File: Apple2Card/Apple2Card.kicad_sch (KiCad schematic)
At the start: 69 parts, among them J1 ICSP, J2 Conn_01x25, J3 Conn_01x25, J4 Conn_01x16, J5 SERCON, J6 WIZNET 5500, SW1 SW_Push, U1 ATmega328P-P, U2 74HCT32, U3 74HCT00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

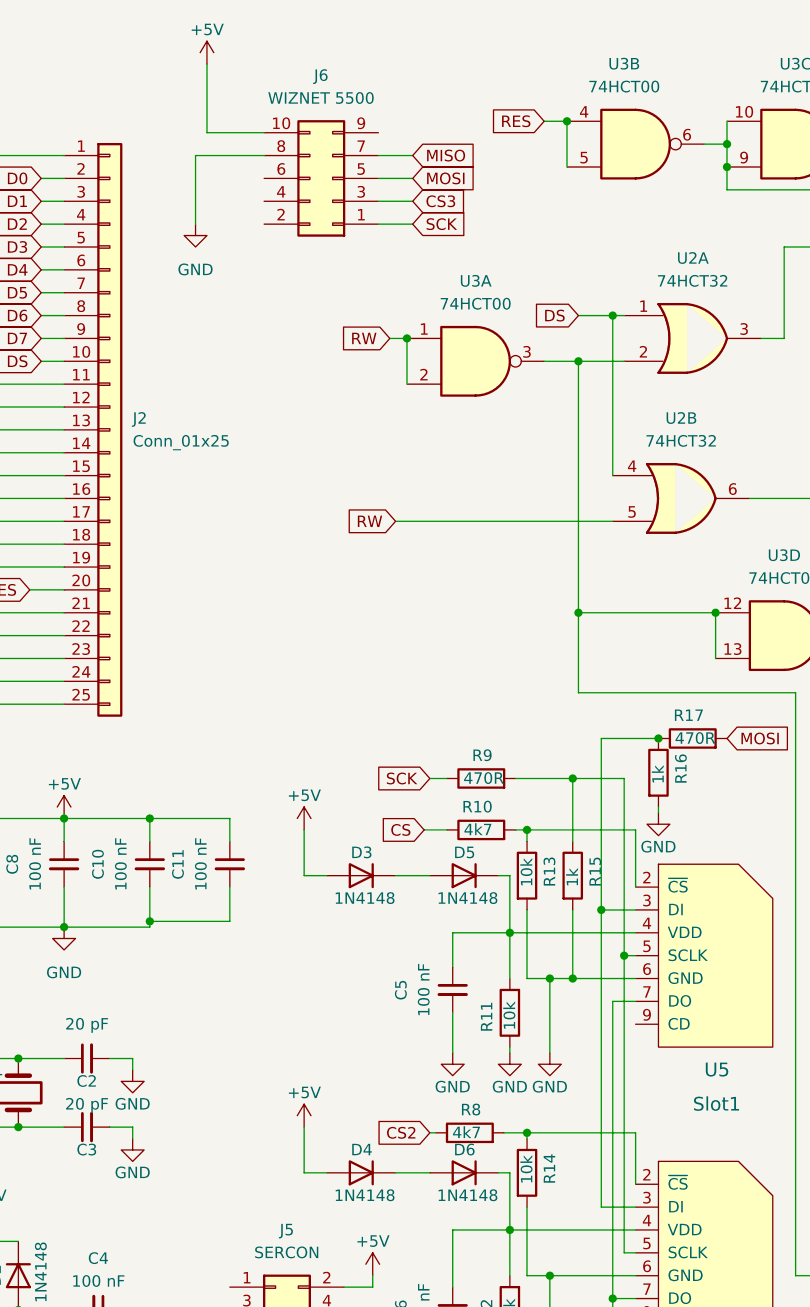
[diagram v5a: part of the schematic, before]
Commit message: Switched around Ethernet output to front side of card, and added access LED for storage
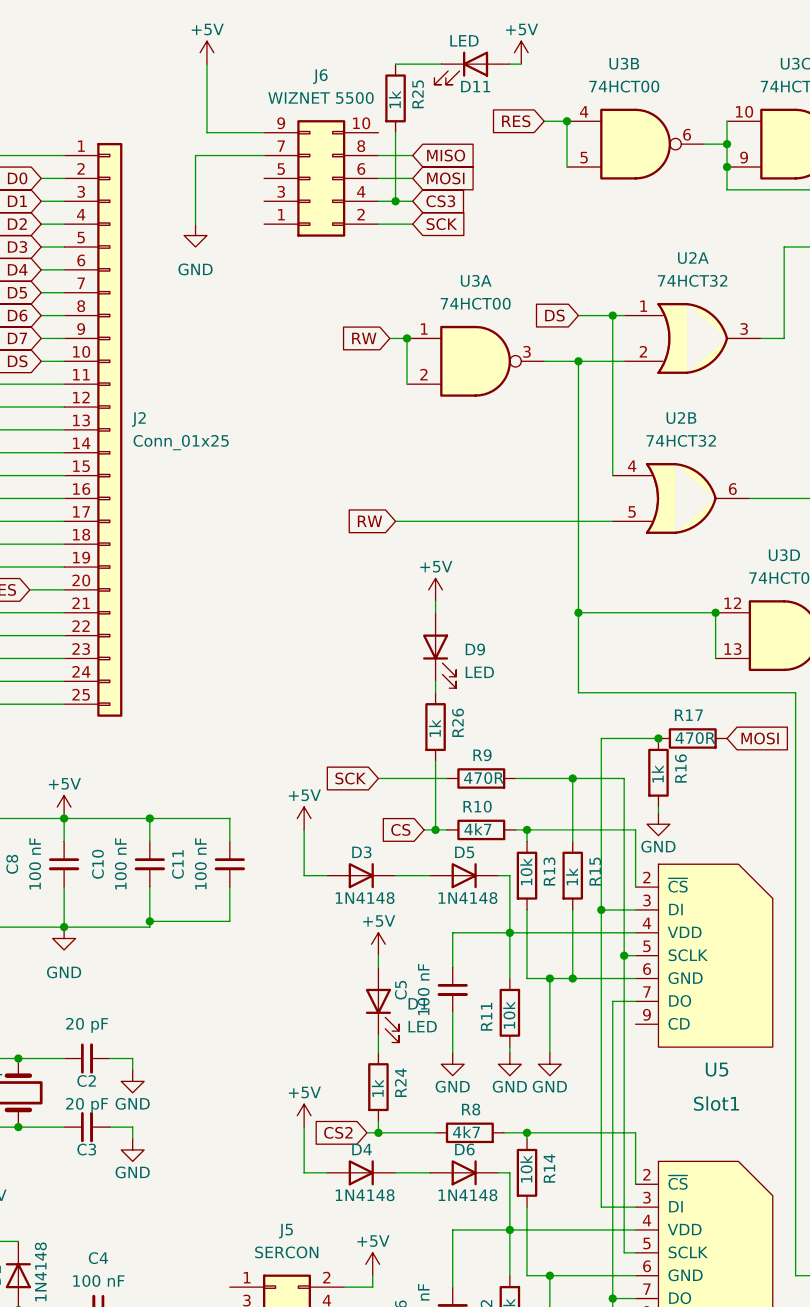
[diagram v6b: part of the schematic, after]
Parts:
- added D1, D11, D9: LED, LED_THT:LED_D3.0mm, symbol Device:LED
- added R24, R25, R26: 1k, Resistor_THT:R_Axial_DIN0207_L6.3mm_D2.5mm_P7.62mm_Horizontal, symbol Device:R
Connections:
- net +5V: now also J6.9 (Pin_9), D1.2 (A), D11.2 (A), D9.2 (A); no longer J6.10 (Pin_10)
- net CS: now also R26.2
- net CS2: now also R24.2
- net CS3: now also J6.4 (Pin_4), R25.2; no longer J6.3 (Pin_3)
- net GND: now also J6.7 (Pin_7); no longer J6.8 (Pin_8)
- net MISO: now also J6.8 (Pin_8); no longer J6.7 (Pin_7)
- net MOSI: now also J6.6 (Pin_6); no longer J6.5 (Pin_5)
- net SCK: now also J6.2 (Pin_2); no longer J6.1 (Pin_1)
- new net: D9.1 (K), R26.1
- new net: D1.1 (K), R24.1
- new net: D11.1 (K), R25.1
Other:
- moved on the sheet: J6

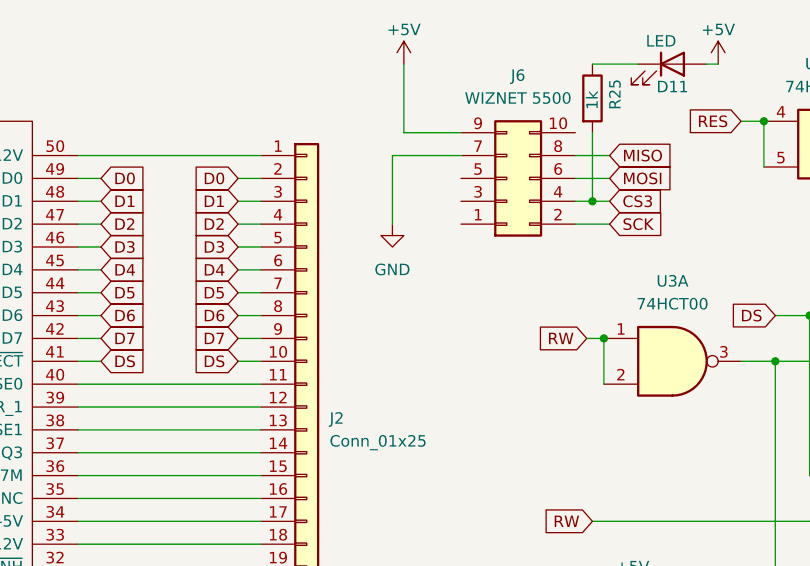
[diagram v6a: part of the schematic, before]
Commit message: Added CS/CS2 pins to feature connector
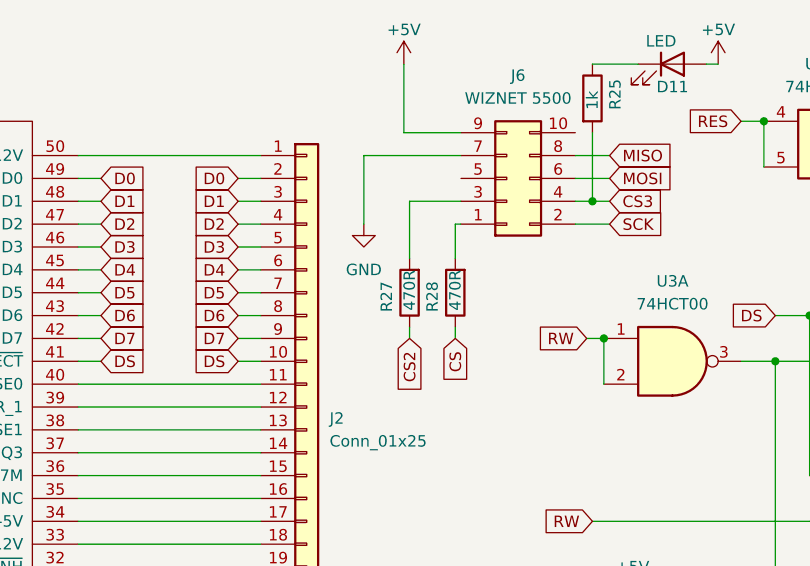
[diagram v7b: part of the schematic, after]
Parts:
- added R27, R28: 470R, Resistor_THT:R_Axial_DIN0207_L6.3mm_D2.5mm_P7.62mm_Horizontal, symbol Device:R
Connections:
- net CS: now also R28.1
- net CS2: now also R27.1
- net at J6.1 (Pin_1): now also R28.2
- net at J6.3 (Pin_3): now also R27.2
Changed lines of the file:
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@@
     (stroke (width 0) (type default) (color 0 0 0 0))
   )
+  (wire (pts (xy 116.84 33.02) (xy 122.555 33.02))
+    (stroke (width 0) (type default) (color 0 0 0 0))
+  )
   (wire (pts (xy 198.12 110.49) (xy 198.12 116.84))
     (stroke (width 0) (type default) (color 0 0 0 0))
@@
     (stroke (width 0) (type default) (color 0 0 0 0))
   )
+  (wire (pts (xy 121.92 46.99) (xy 121.92 48.26))
+    (stroke (width 0) (type default) (color 0 0 0 0))
+  )
   (wire (pts (xy 248.92 111.76) (xy 254 111.76))
     (stroke (width 0) (type default) (color 0 0 0 0))
@@
     (stroke (width 0) (type default) (color 0 0 0 0))
   )
-  (wire (pts (xy 114.935 27.94) (xy 122.555 27.94))
+  (wire (pts (xy 111.76 27.94) (xy 122.555 27.94))
     (stroke (width 0) (type default) (color 0 0 0 0))
   )
@@
     (stroke (width 0) (type default) (color 0 0 0 0))
   )
-  (wire (pts (xy 114.935 35.56) (xy 114.935 27.94))
+  (wire (pts (xy 111.76 35.56) (xy 111.76 27.94))
     (stroke (width 0) (type default) (color 0 0 0 0))
   )
@@
     (stroke (width 0) (type default) (color 0 0 0 0))
   )
+  (wire (pts (xy 116.84 46.99) (xy 116.84 48.26))
+    (stroke (width 0) (type default) (color 0 0 0 0))
+  )
   (wire (pts (xy 80.01 60.96) (xy 100.33 60.96))
     (stroke (width 0) (type default) (color 0 0 0 0))
@@
     (stroke (width 0) (type default) (color 0 0 0 0))
   )
+  (wire (pts (xy 121.92 35.56) (xy 122.555 35.56))
+    (stroke (width 0) (type default) (color 0 0 0 0))
+  )
   (wire (pts (xy 274.32 124.46) (xy 276.86 124.46))
     (stroke (width 0) (type default) (color 0 0 0 0))
@@
     (stroke (width 0) (type default) (color 0 0 0 0))
   )
+  (wire (pts (xy 116.84 39.37) (xy 116.84 33.02))
+    (stroke (width 0) (type default) (color 0 0 0 0))
+  )
   (wire (pts (xy 224.155 142.24) (xy 254 142.24))
     (stroke (width 0) (type default) (color 0 0 0 0))
@@
     (stroke (width 0) (type default) (color 0 0 0 0))
   )
+  (wire (pts (xy 121.92 39.37) (xy 121.92 35.56))
+    (stroke (width 0) (type default) (color 0 0 0 0))
+  )
   (wire (pts (xy 117.475 163.83) (xy 118.745 163.83))
     (stroke (width 0) (type default) (color 0 0 0 0))
@@
     )
   )
+  (global_label "CS2" (shape input) (at 116.84 48.26 270) (fields_autoplaced)
+    (effects (font (size 1.27 1.27)) (justify right))
+    (property "Intersheet References" "${INTERSHEET_REFS}" (id 0) (at 116.9194 54.2732 90)
+      (effects (font (size 1.27 1.27)) (justify right) hide)
+    )
+  )
   (global_label "MISO" (shape input) (at 73.66 128.27 0) (fields_autoplaced)
     (effects (font (size 1.27 1.27)) (justify left))
@@
     )
   )
+  (global_label "CS" (shape input) (at 121.92 48.26 270) (fields_autoplaced)
+    (effects (font (size 1.27 1.27)) (justify right))
+    (property "Intersheet References" "${INTERSHEET_REFS}" (id 0) (at 121.9994 53.0637 90)
+      (effects (font (size 1.27 1.27)) (justify right) hide)
+    )
+  )
   (global_label "RW" (shape input) (at 49.53 71.12 180) (fields_autoplaced)
     (effects (font (size 1.27 1.27)) (justify right))
@@
     (pin "6")
   )
-  (symbol (lib_id "power:GND") (at 114.935 35.56 0) (unit 1)
+  (symbol (lib_id "power:GND") (at 111.76 35.56 0) (unit 1)
     (in_bom yes) (on_board yes) (fields_autoplaced)
-    (property "Reference" "#PWR0116" (id 0) (at 114.935 41.91 0)
+    (property "Reference" "#PWR0116" (id 0) (at 111.76 41.91 0)
       (effects (font (size 1.27 1.27)) hide)
     )
-    (property "Value" "GND" (id 1) (at 114.935 40.64 0))
-    (property "Footprint" "" (id 2) (at 114.935 35.56 0)
+    (property "Value" "GND" (id 1) (at 111.76 40.64 0))
+    (property "Footprint" "" (id 2) (at 111.76 35.56 0)
       (effects (font (size 1.27 1.27)) hide)
     )
-    (property "Datasheet" "" (id 3) (at 114.935 35.56 0)
+    (property "Datasheet" "" (id 3) (at 111.76 35.56 0)
       (effects (font (size 1.27 1.27)) hide)
     )
@@
     (pin "1")
   )
+  (symbol (lib_id "Device:R") (at 121.92 43.18 180) (unit 1)
+    (in_bom yes) (on_board yes)
+    (property "Reference" "R28" (id 0) (at 119.38 41.91 90)
+      (effects (font (size 1.27 1.27)) (justify left))
+    )
+    (property "Value" "470R" (id 1) (at 121.92 40.64 90)
+      (effects (font (size 1.27 1.27)) (justify left))
+    )
+    (property "Footprint" "Resistor_THT:R_Axial_DIN0207_L6.3mm_D2.5mm_P7.62mm_Horizontal" (id 2) (at 123.698 43.18 90)
+      (effects (font (size 1.27 1.27)) hide)
+    )
+    (property "Datasheet" "~" (id 3) (at 121.92 43.18 0)
+      (effects (font (size 1.27 1.27)) hide)
+    )
+    (pin "1")
+    (pin "2")
+  )
+  (symbol (lib_id "Device:R") (at 116.84 43.18 180) (unit 1)
+    (in_bom yes) (on_board yes)
+    (property "Reference" "R27" (id 0) (at 114.3 41.91 90)
+      (effects (font (size 1.27 1.27)) (justify left))
+    )
+    (property "Value" "470R" (id 1) (at 116.84 40.64 90)
+      (effects (font (size 1.27 1.27)) (justify left))
+    )
+    (property "Footprint" "Resistor_THT:R_Axial_DIN0207_L6.3mm_D2.5mm_P7.62mm_Horizontal" (id 2) (at 118.618 43.18 90)
+      (effects (font (size 1.27 1.27)) hide)
+    )
+    (property "Datasheet" "~" (id 3) (at 116.84 43.18 0)
+      (effects (font (size 1.27 1.27)) hide)
+    )
+    (pin "1")
+    (pin "2")
+  )
   (symbol (lib_id "power:GND") (at 40.64 96.52 0) (unit 1)
     (in_bom yes) (on_board yes) (fields_autoplaced)
@@
       (reference "R26") (unit 1) (value "1k") (footprint "Resistor_THT:R_Axial_DIN0207_L6.3mm_D2.5mm_P7.62mm_Horizontal")
     )
+    (path "/2f0d9ca5-4789-400f-a68c-241118792eed"
+      (reference "R27") (unit 1) (value "470R") (footprint "Resistor_THT:R_Axial_DIN0207_L6.3mm_D2.5mm_P7.62mm_Horizontal")
+    )
+    (path "/2dbfff57-2e19-4938-b7b7-2d2edd4a4b8f"
+      (reference "R28") (unit 1) (value "470R") (footprint "Resistor_THT:R_Axial_DIN0207_L6.3mm_D2.5mm_P7.62mm_Horizontal")
+    )
     (path "/e4b49c93-8dc9-4648-904a-94b3737a600f"

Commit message: Added picture
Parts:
- R27, R28: value 470R -> 4k7
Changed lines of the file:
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@@
       (effects (font (size 1.27 1.27)) (justify left))
     )
-    (property "Value" "470R" (id 1) (at 121.92 40.64 90)
+    (property "Value" "4k7" (id 1) (at 121.92 40.64 90)
       (effects (font (size 1.27 1.27)) (justify left))
     )
@@
       (effects (font (size 1.27 1.27)) (justify left))
     )
-    (property "Value" "470R" (id 1) (at 116.84 40.64 90)
+    (property "Value" "4k7" (id 1) (at 116.84 40.64 90)
       (effects (font (size 1.27 1.27)) (justify left))
     )
@@
     )
     (path "/2f0d9ca5-4789-400f-a68c-241118792eed"
-      (reference "R27") (unit 1) (value "470R") (footprint "Resistor_THT:R_Axial_DIN0207_L6.3mm_D2.5mm_P7.62mm_Horizontal")
+      (reference "R27") (unit 1) (value "4k7") (footprint "Resistor_THT:R_Axial_DIN0207_L6.3mm_D2.5mm_P7.62mm_Horizontal")
     )
     (path "/2dbfff57-2e19-4938-b7b7-2d2edd4a4b8f"
-      (reference "R28") (unit 1) (value "470R") (footprint "Resistor_THT:R_Axial_DIN0207_L6.3mm_D2.5mm_P7.62mm_Horizontal")
+      (reference "R28") (unit 1) (value "4k7") (footprint "Resistor_THT:R_Axial_DIN0207_L6.3mm_D2.5mm_P7.62mm_Horizontal")
     )
     (path "/e4b49c93-8dc9-4648-904a-94b3737a600f"
